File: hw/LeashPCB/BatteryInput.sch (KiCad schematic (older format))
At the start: 11 parts, among them J201 1020-1, J202 1076-1, J203 1076-1, Q201 CSD18501Q5A, U201 LM74610Q

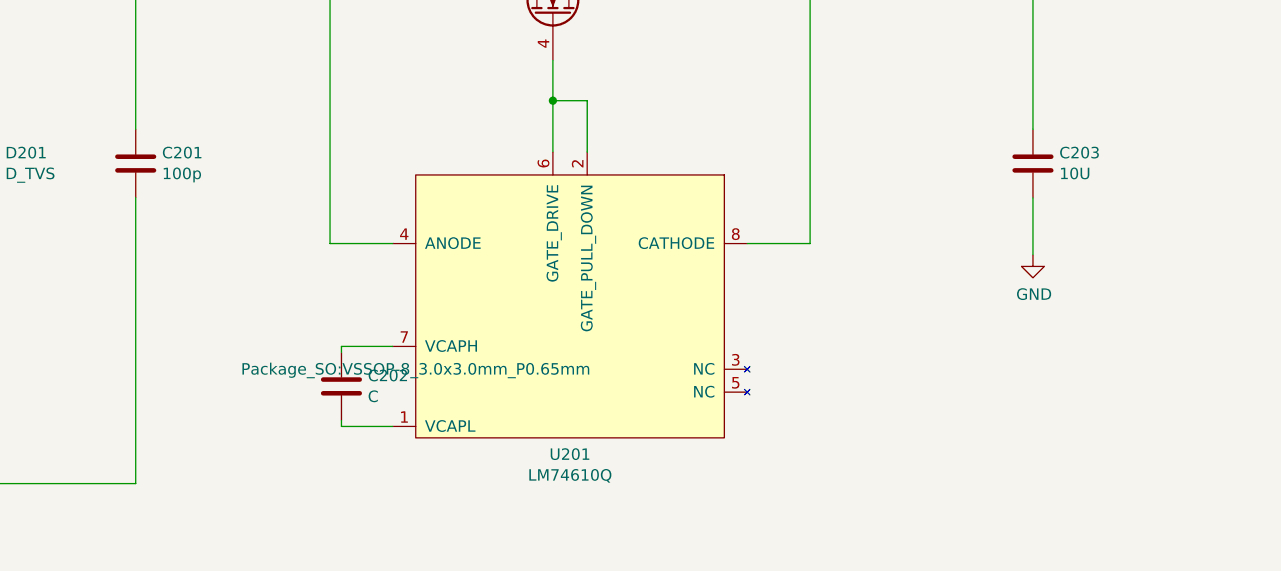
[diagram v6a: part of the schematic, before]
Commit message: Adding part info for ordering components
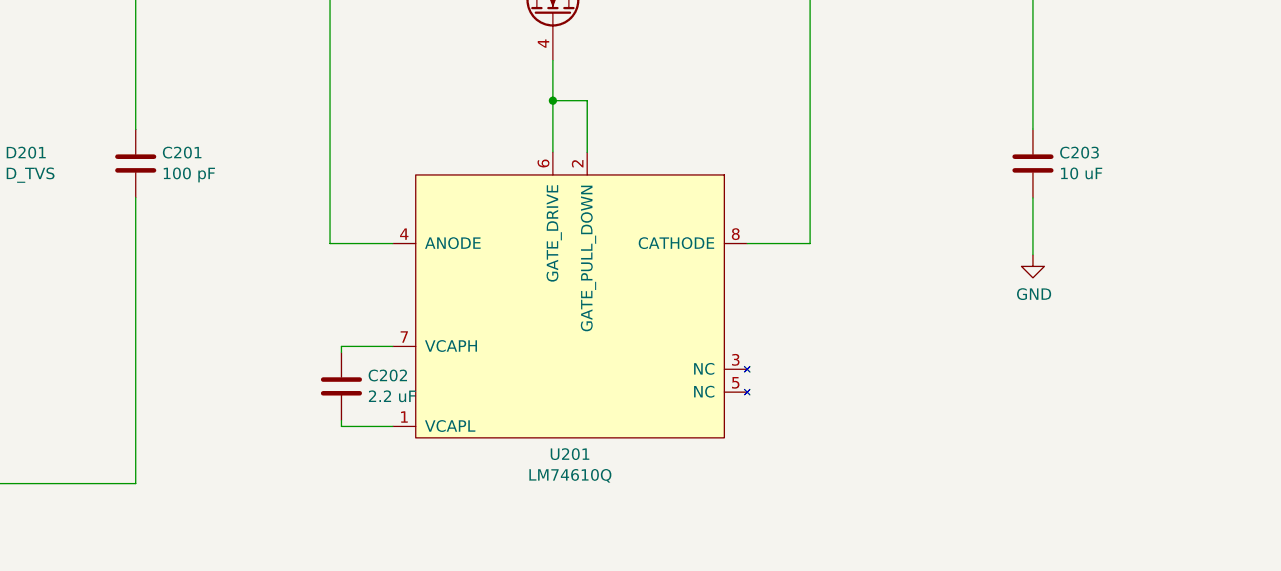
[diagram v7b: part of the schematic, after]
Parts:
- C201: value 100p -> 100 pF; Description (none) -> CAP CER 100PF 50V C0G/NPO 0402; Link1 (none) -> https://www.digikey.com/product-detail/en/yageo/CC0402JRNPO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; MPN1 (none) -> CC0402JRNPO9BN101; Standard Price (none) -> $0.00346; Vendor1 (none) -> Yageo
- C202: value C -> 2.2 uF; Description (none) -> CAP CER 2.2UF 10V X5R 0402; Link1 (none) -> https://www.digikey.com/product-detail/en/taiyo-yuden/LMK10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; MPN1 (none) -> LMK105BJ225MV-F; Standard Price (none) -> $0.01210; Vendor1 (none) -> Taiyo Yuden
- C203: value 10U -> 10 uF; Description (none) -> CAP CER 10UF 6.3V X5R 0603; Link1 (none) -> https://www.digikey.com/product-detail/en/samsung-electro-m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; MPN1 (none) -> CL10A106MQ8NNNC; Standard Price (none) -> $0.02215
- D201: Description (none) -> TVS DIODE 20V 34V DFN1006-2; Link1 (none) -> https://www.digikey.com/product-detail/en/diodes-incorporat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; MPN1 (none) -> D20V0L1B2LP-7B; Standard Price (none) -> $0.03400; Vendor1 (none) -> Diodes Incorporated
- J201: Description (none) -> BATTERY CONTACT SPRING MULTI SMD; Link1 (none) -> https://www.digikey.com/product-detail/en/keystone-electron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; MPN1 (none) -> 1020-1; Standard Price 0.05 -> $0.05; Vendor1 (none) -> Keystone Electronics
- J202: Description (none) -> BATT CONTACT SOLID MULTI SMD TAB; Link1 (none) -> https://www.digikey.com/product-detail/en/keystone-electron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; MPN1 (none) -> 1076-1; Standard Price 0.05 -> $0.05; Vendor1 (none) -> Keystone Electronics
- J203: Description (none) -> BATT CONTACT SOLID MULTI SMD TAB; Link1 (none) -> https://www.digikey.com/product-detail/en/keystone-electron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; MPN1 (none) -> 1076-1; Population (none) -> DNP; Standard Price 0.05 -> $0.05; Vendor1 (none) -> Keystone Electronics
- R201, R203: Description (none) -> RES 0 OHM JUMPER 1/16W 0402; Link1 (none) -> https://www.digikey.com/product-detail/en/stackpole-electro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; MPN1 (none) -> RMCF0402ZT0R00; Standard Price (none) -> $0.00127; Vendor1 (none) -> Stackpole Electronics Inc
- U201: Description (none) -> IC SMART DIODE CTLR 8VSSOP; Link1 http://www.ti.com/product/LM74610-Q1 -> https://www.digikey.com/product-detail/en/texas-instruments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
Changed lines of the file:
@@
 F 2 "leash:1076-1" H 4025 3725 50  0001 C CNN
 F 3 "" H 4025 3725 50  0001 C CNN
-F 4 "0.05" H 4025 3725 50  0001 C CNN "Standard Price"
+F 4 "$0.05" H 4025 3725 50  0001 C CNN "Standard Price"
+F 5 "BATT CONTACT SOLID MULTI SMD TAB" H 4025 3725 50  0001 C CNN "Description"
+F 6 "https://www.digikey.com/product-detail/en/keystone-electronics/1076-1/36-1076-1-ND/8347182" H 4025 3725 50  0001 C CNN "Link1"
+F 7 "1076-1" H 4025 3725 50  0001 C CNN "MPN1"
+F 8 "Keystone Electronics" H 4025 3725 50  0001 C CNN "Vendor1"
 	1    4025 3725
 	0    -1   -1   0
@@
 F 2 "leash:1020-1" H 4025 1975 50  0001 C CNN
 F 3 "" H 4025 1975 50  0001 C CNN
-F 4 "0.05" H 4025 1975 50  0001 C CNN "Standard Price"
+F 4 "$0.05" H 4025 1975 50  0001 C CNN "Standard Price"
+F 5 "BATTERY CONTACT SPRING MULTI SMD" H 4025 1975 50  0001 C CNN "Description"
+F 6 "https://www.digikey.com/product-detail/en/keystone-electronics/1020-1/36-1020-1-ND/5118841" H 4025 1975 50  0001 C CNN "Link1"
+F 7 "1020-1" H 4025 1975 50  0001 C CNN "MPN1"
+F 8 "Keystone Electronics" H 4025 1975 50  0001 C CNN "Vendor1"
 	1    4025 1975
 	0    1    1    0
@@
 F 2 "Diode_SMD:D_0402_1005Metric" H 5900 2525 50  0001 C CNN
 F 3 "~" H 5900 2525 50  0001 C CNN
+F 4 "TVS DIODE 20V 34V DFN1006-2" H 5900 2525 50  0001 C CNN "Description"
+F 5 "https://www.digikey.com/product-detail/en/diodes-incorporated/D20V0L1B2LP-7B/D20V0L1B2LP-7BDICT-ND/6052571" H 5900 2525 50  0001 C CNN "Link1"
+F 6 "D20V0L1B2LP-7B" H 5900 2525 50  0001 C CNN "MPN1"
+F 7 "$0.03400" H 5900 2525 50  0001 C CNN "Standard Price"
+F 8 "Diodes Incorporated" H 5900 2525 50  0001 C CNN "Vendor1"
 	1    5900 2525
 	0    1    1    0
@@
 P 6550 2525
 F 0 "C201" H 6665 2571 50  0000 L CNN
-F 1 "100p" H 6665 2480 50  0000 L CNN
+F 1 "100 pF" H 6665 2480 50  0000 L CNN
 F 2 "Capacitor_SMD:C_0402_1005Metric" H 6588 2375 50  0001 C CNN
 F 3 "~" H 6550 2525 50  0001 C CNN
+F 4 "CAP CER 100PF 50V C0G/NPO 0402" H 6550 2525 50  0001 C CNN "Description"
+F 5 "https://www.digikey.com/product-detail/en/yageo/CC0402JRNPO9BN101/311-1024-1-ND/302941" H 6550 2525 50  0001 C CNN "Link1"
+F 6 "CC0402JRNPO9BN101" H 6550 2525 50  0001 C CNN "MPN1"
+F 7 "$0.00346" H 6550 2525 50  0001 C CNN "Standard Price"
+F 8 "Yageo" H 6550 2525 50  0001 C CNN "Vendor1"
 	1    6550 2525
 	1    0    0    -1
@@
 P 7450 3500
 F 0 "C202" H 7565 3546 50  0000 L CNN
-F 1 "C" H 7565 3455 50  0000 L CNN
+F 1 "2.2 uF" H 7565 3455 50  0000 L CNN
 F 2 "Capacitor_SMD:C_0402_1005Metric" H 7488 3350 50  0001 C CNN
 F 3 "~" H 7450 3500 50  0001 C CNN
+F 4 "CAP CER 2.2UF 10V X5R 0402" H 7450 3500 50  0001 C CNN "Description"
+F 5 "https://www.digikey.com/product-detail/en/taiyo-yuden/LMK105BJ225MV-F/587-3153-1-ND/2774767" H 7450 3500 50  0001 C CNN "Link1"
+F 6 "LMK105BJ225MV-F" H 7450 3500 50  0001 C CNN "MPN1"
+F 7 "$0.01210" H 7450 3500 50  0001 C CNN "Standard Price"
+F 8 "Taiyo Yuden" H 7450 3500 50  0001 C CNN "Vendor1"
 	1    7450 3500
 	1    0    0    -1
@@
 F 0 "U201" H 8450 2452 50  0000 C CNN
 F 1 "LM74610Q" H 8450 2361 50  0000 C CNN
-F 2 "Package_SO:VSSOP-8_3.0x3.0mm_P0.65mm" H 7775 2825 50  0000 C CNN
+F 2 "Package_SO:VSSOP-8_3.0x3.0mm_P0.65mm" H 7775 2825 50  0001 C CNN
 F 3 "http://www.ti.com/lit/ds/symlink/lm74610-q1.pdf" H 7775 2825 50  0001 C CNN
 F 4 "LM74610QDGKRQ1" H 8525 3125 50  0001 C CNN "MPN1"
-F 5 "http://www.ti.com/product/LM74610-Q1" H 8525 3125 50  0001 C CNN "Link1"
+F 5 "https://www.digikey.com/product-detail/en/texas-instruments/LM74610QDGKRQ1/296-43067-1-ND/5722225" H 8525 3125 50  0001 C CNN "Link1"
 F 6 "Texas Instruments" H 8525 3125 50  0001 C CNN "Vendor1"
 F 7 "0.23" H 8525 3125 50  0001 C CNN "Standard Price"
+F 8 "IC SMART DIODE CTLR 8VSSOP" H 8525 3125 50  0001 C CNN "Description"
 	1    8525 3125
 	1    0    0    -1
@@
 P 10475 2525
 F 0 "C203" H 10590 2571 50  0000 L CNN
-F 1 "10U" H 10590 2480 50  0000 L CNN
+F 1 "10 uF" H 10590 2480 50  0000 L CNN
 F 2 "Capacitor_SMD:C_0603_1608Metric" H 10513 2375 50  0001 C CNN
 F 3 "~" H 10475 2525 50  0001 C CNN
+F 4 "CAP CER 10UF 6.3V X5R 0603" H 10475 2525 50  0001 C CNN "Description"
+F 5 "https://www.digikey.com/product-detail/en/samsung-electro-mechanics/CL10A106MQ8NNNC/1276-1119-1-ND/3889205" H 10475 2525 50  0001 C CNN "Link1"
+F 6 "CL10A106MQ8NNNC" H 10475 2525 50  0001 C CNN "MPN1"
+F 7 "$0.02215" H 10475 2525 50  0001 C CNN "Standard Price"
 	1    10475 2525
 	1    0    0    -1
@@
 F 2 "Resistor_SMD:R_0402_1005Metric" V 12705 1775 50  0001 C CNN
 F 3 "~" H 12775 1775 50  0001 C CNN
+F 4 "RES 0 OHM JUMPER 1/16W 0402" H 12775 1775 50  0001 C CNN "Description"
+F 5 "https://www.digikey.com/product-detail/en/stackpole-electronics-inc/RMCF0402ZT0R00/RMCF0402ZT0R00TR-ND/1756905" H 12775 1775 50  0001 C CNN "Link1"
+F 6 "RMCF0402ZT0R00" H 12775 1775 50  0001 C CNN "MPN1"
+F 7 "$0.00127	" H 12775 1775 50  0001 C CNN "Standard Price"
+F 8 "Stackpole Electronics Inc" H 12775 1775 50  0001 C CNN "Vendor1"
 	1    12775 1775
 	0    1    1    0
@@
 F 2 "leash:1076-1" H 3325 3725 50  0001 C CNN
 F 3 "" H 3325 3725 50  0001 C CNN
-F 4 "0.05" H 3325 3725 50  0001 C CNN "Standard Price"
+F 4 "$0.05" H 3325 3725 50  0001 C CNN "Standard Price"
+F 5 "BATT CONTACT SOLID MULTI SMD TAB" H 3325 3725 50  0001 C CNN "Description"
+F 6 "https://www.digikey.com/product-detail/en/keystone-electronics/1076-1/36-1076-1-ND/8347182" H 3325 3725 50  0001 C CNN "Link1"
+F 7 "1076-1" H 3325 3725 50  0001 C CNN "MPN1"
+F 8 "DNP" H 3325 3725 50  0001 C CNN "Population"
+F 9 "Keystone Electronics" H 3325 3725 50  0001 C CNN "Vendor1"
 	1    3325 3725
 	0    -1   -1   0
@@
 F 3 "~" H 8350 1125 50  0001 C CNN
 F 4 "DNP" V 8250 1075 50  0000 L CNN "Population"
+F 5 "RES 0 OHM JUMPER 1/16W 0402" H 8350 1125 50  0001 C CNN "Description"
+F 6 "https://www.digikey.com/product-detail/en/stackpole-electronics-inc/RMCF0402ZT0R00/RMCF0402ZT0R00TR-ND/1756905" H 8350 1125 50  0001 C CNN "Link1"
+F 7 "RMCF0402ZT0R00" H 8350 1125 50  0001 C CNN "MPN1"
+F 8 "$0.00127	" H 8350 1125 50  0001 C CNN "Standard Price"
+F 9 "Stackpole Electronics Inc" H 8350 1125 50  0001 C CNN "Vendor1"
 	1    8350 1125
 	0    1    1    0

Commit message: Finished added components and generated BOM for ordering all parts
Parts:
- C201: Short Description (none) -> CAP CER 100PF 50V C0G/NPO 0402
- C202: Short Description (none) -> CAP CER 2.2UF 10V X5R 0402
- C203: Short Description (none) -> CAP CER 10UF 6.3V X5R 0603
- D201: Short Description (none) -> TVS DIODE 20V 34V DFN1006-2
- J201: Short Description (none) -> BATTERY CONTACT SPRING MULTI SMD
- J202, J203: Short Description (none) -> BATT CONTACT SOLID MULTI SMD TAB
- Q201: Description (none) -> MOSFET N-CH 40V 8SON; Link1 (none) -> https://www.digikey.com/product-detail/en/texas-instruments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; Short Description (none) -> MOSFET N-CH 40V 8SON; Standard Price 0.16 -> $0.16; Vendor1 (none) -> Texas Instruments
- R201, R203: Short Description (none) -> RES 0 OHM JUMPER 1/16W 0402; Standard Price $0.00127 -> $0.00127
- U201: Short Description (none) -> IC SMART DIODE CTLR 8VSSOP
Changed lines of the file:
@@
 Sheet 2 10
 Title "BeagleDust Leash PCB"
-Date "2019-07-22"
-Rev "1"
+Date "2019-08-12"
+Rev "A"
 Comp "Beagleboard.org"
 Comment1 "Schematic designed by Analog Life, LLC"
@@
 F 7 "1076-1" H 4025 3725 50  0001 C CNN "MPN1"
 F 8 "Keystone Electronics" H 4025 3725 50  0001 C CNN "Vendor1"
+F 9 "BATT CONTACT SOLID MULTI SMD TAB" H 4025 3725 50  0001 C CNN "Short Description"
 	1    4025 3725
 	0    -1   -1   0
@@
 F 7 "1020-1" H 4025 1975 50  0001 C CNN "MPN1"
 F 8 "Keystone Electronics" H 4025 1975 50  0001 C CNN "Vendor1"
+F 9 "BATTERY CONTACT SPRING MULTI SMD" H 4025 1975 50  0001 C CNN "Short Description"
 	1    4025 1975
 	0    1    1    0
@@
 F 7 "$0.03400" H 5900 2525 50  0001 C CNN "Standard Price"
 F 8 "Diodes Incorporated" H 5900 2525 50  0001 C CNN "Vendor1"
+F 9 "TVS DIODE 20V 34V DFN1006-2" H 5900 2525 50  0001 C CNN "Short Description"
 	1    5900 2525
 	0    1    1    0
@@
 F 7 "$0.00346" H 6550 2525 50  0001 C CNN "Standard Price"
 F 8 "Yageo" H 6550 2525 50  0001 C CNN "Vendor1"
+F 9 "CAP CER 100PF 50V C0G/NPO 0402" H 6550 2525 50  0001 C CNN "Short Description"
 	1    6550 2525
 	1    0    0    -1
@@
 F 7 "$0.01210" H 7450 3500 50  0001 C CNN "Standard Price"
 F 8 "Taiyo Yuden" H 7450 3500 50  0001 C CNN "Vendor1"
+F 9 "CAP CER 2.2UF 10V X5R 0402" H 7450 3500 50  0001 C CNN "Short Description"
 	1    7450 3500
 	1    0    0    -1
@@
 F 7 "0.23" H 8525 3125 50  0001 C CNN "Standard Price"
 F 8 "IC SMART DIODE CTLR 8VSSOP" H 8525 3125 50  0001 C CNN "Description"
+F 9 "IC SMART DIODE CTLR 8VSSOP" H 8525 3125 50  0001 C CNN "Short Description"
 	1    8525 3125
 	1    0    0    -1
@@
 F 6 "CL10A106MQ8NNNC" H 10475 2525 50  0001 C CNN "MPN1"
 F 7 "$0.02215" H 10475 2525 50  0001 C CNN "Standard Price"
+F 8 "CAP CER 10UF 6.3V X5R 0603" H 10475 2525 50  0001 C CNN "Short Description"
 	1    10475 2525
 	1    0    0    -1
@@
 F 2 "Package_TO_SOT_SMD:TDSON-8-1" H 8575 1800 50  0001 L CIN
 F 3 "http://www.ti.com/lit/gpn/csd18501q5a" V 8375 1875 50  0001 L CNN
-F 4 "0.16" H 8375 1875 50  0001 C CNN "Standard Price"
+F 4 "$0.16" H 8375 1875 50  0001 C CNN "Standard Price"
 F 5 "CSD18501Q5A" H 8375 1875 50  0001 C CNN "MPN1"
+F 6 "MOSFET N-CH 40V 8SON" H 8375 1875 50  0001 C CNN "Description"
+F 7 "https://www.digikey.com/product-detail/en/texas-instruments/CSD18501Q5A/296-30570-1-ND/3478030" H 8375 1875 50  0001 C CNN "Link1"
+F 8 "Texas Instruments" H 8375 1875 50  0001 C CNN "Vendor1"
+F 9 "MOSFET N-CH 40V 8SON" H 8375 1875 50  0001 C CNN "Short Description"
 	1    8375 1875
 	0    1    -1   0
@@
 F 5 "https://www.digikey.com/product-detail/en/stackpole-electronics-inc/RMCF0402ZT0R00/RMCF0402ZT0R00TR-ND/1756905" H 12775 1775 50  0001 C CNN "Link1"
 F 6 "RMCF0402ZT0R00" H 12775 1775 50  0001 C CNN "MPN1"
-F 7 "$0.00127	" H 12775 1775 50  0001 C CNN "Standard Price"
+F 7 "$0.00127" H 12775 1775 50  0001 C CNN "Standard Price"
 F 8 "Stackpole Electronics Inc" H 12775 1775 50  0001 C CNN "Vendor1"
+F 9 "RES 0 OHM JUMPER 1/16W 0402" H 12775 1775 50  0001 C CNN "Short Description"
 	1    12775 1775
 	0    1    1    0
@@
 F 8 "DNP" H 3325 3725 50  0001 C CNN "Population"
 F 9 "Keystone Electronics" H 3325 3725 50  0001 C CNN "Vendor1"
+F 10 "BATT CONTACT SOLID MULTI SMD TAB" H 3325 3725 50  0001 C CNN "Short Description"
 	1    3325 3725
 	0    -1   -1   0
@@
 F 6 "https://www.digikey.com/product-detail/en/stackpole-electronics-inc/RMCF0402ZT0R00/RMCF0402ZT0R00TR-ND/1756905" H 8350 1125 50  0001 C CNN "Link1"
 F 7 "RMCF0402ZT0R00" H 8350 1125 50  0001 C CNN "MPN1"
-F 8 "$0.00127	" H 8350 1125 50  0001 C CNN "Standard Price"
+F 8 "$0.00127" H 8350 1125 50  0001 C CNN "Standard Price"
 F 9 "Stackpole Electronics Inc" H 8350 1125 50  0001 C CNN "Vendor1"
+F 10 "RES 0 OHM JUMPER 1/16W 0402" H 8350 1125 50  0001 C CNN "Short Description"
 	1    8350 1125
 	0    1    1    0
